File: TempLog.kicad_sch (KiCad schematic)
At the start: 50 parts, among them J1 1.27, 2x5, Male, TH, J2 Conn_01x02, J3 Conn_01x03, J5 Conn_01x02, J6 USB4105-GF-A-060, Q1 DMP6350S, SW1 SMD_4.6x2.8mm_h1.9mm, SW2 SMD_4.6x2.8mm_h1.9mm, U1 STM32F030C8Tx, U2 GD25Q16CSJGR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

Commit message: Added PDFs
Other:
- company: (none) -> Uri Tech
- title: (none) -> Temperature Logger - TempLog - V0

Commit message: Updated project to Kicad 9
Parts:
- U2: value GD25Q16CSJGR -> GD25Q16CSJGR
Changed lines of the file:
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@@
 (kicad_sch
-	(version 20231120)
+	(version 20250114)
 	(generator "eeschema")
-	(generator_version "8.0")
+	(generator_version "9.0")
 	(paper "A3")
 	(title_block
@@
 		(company "Uri Tech")
 	)
+	(rectangle
+		(start 109.982 11.938)
+		(end 210.058 84.836)
+		(stroke
+			(width 0)
+			(type default)
+		)
+		(fill
+			(type none)
+		)
+	)
+	(rectangle
+		(start 11.938 84.836)
+		(end 210.058 160.02)
+		(stroke
+			(width 0)
+			(type default)
+		)
+		(fill
+			(type none)
+		)
+	)
+	(rectangle
+		(start 11.938 11.938)
+		(end 109.982 84.836)
+		(stroke
+			(width 0)
+			(type default)
+		)
+		(fill
+			(type none)
+		)
+	)
+	(rectangle
+		(start 299.974 84.836)
+		(end 407.924 252.984)
+		(stroke
+			(width 0)
+			(type default)
+		)
+		(fill
+			(type none)
+		)
+	)
+	(rectangle
+		(start 11.938 160.02)
+		(end 299.974 284.988)
+		(stroke
+			(width 0)
+			(type default)
+		)
+		(fill
+			(type none)
+		)
+	)
+	(rectangle
+		(start 210.058 84.836)
+		(end 299.974 160.02)
+		(stroke
+			(width 0)
+			(type default)
+		)
+		(fill
+			(type none)
+		)
+	)
+	(rectangle
+		(start 210.058 11.938)
+		(end 299.974 84.836)
+		(stroke
+			(width 0)
+			(type default)
+		)
+		(fill
+			(type none)
+		)
+	)
+	(text "Power Supply"
+		(exclude_from_sim no)
+		(at 108.966 93.218 0)
+		(effects
+			(font
+				(size 1.27 1.27)
+			)
+		)
+	)
+	(text "Programming Interface"
+		(exclude_from_sim no)
+		(at 251.206 94.234 0)
+		(effects
+			(font
+				(size 1.27 1.27)
+			)
+		)
+	)
+	(text "GND"
+		(exclude_from_sim no)
+		(at 46.99 54.61 0)
+		(effects
+			(font
+				(size 1.27 1.27)
+			)
+		)
+	)
+	(text "LEDs"
+		(exclude_from_sim no)
+		(at 154.686 21.844 0)
+		(effects
+			(font
+				(size 1.27 1.27)
+			)
+		)
+	)
+	(text "Microcontroller"
+		(exclude_from_sim no)
+		(at 58.928 167.386 0)
+		(effects
+			(font
+				(size 1.27 1.27)
+			)
+		)
+	)
+	(text "Decoupling Capacitors"
+		(exclude_from_sim no)
+		(at 146.558 231.902 0)
+		(effects
+			(font
+				(size 1.27 1.27)
+			)
+		)
+	)
+	(text "Thermistor Circuit"
+		(exclude_from_sim no)
+		(at 355.346 94.996 0)
+		(effects
+			(font
+				(size 1.27 1.27)
+			)
+		)
+	)
+	(text "TX"
+		(exclude_from_sim no)
+		(at 46.228 52.07 0)
+		(effects
+			(font
+				(size 1.27 1.27)
+			)
+		)
+	)
+	(text "RX"
+		(exclude_from_sim no)
+		(at 46.482 49.53 0)
+		(effects
+			(font
+				(size 1.27 1.27)
+			)
+		)
+	)
+	(text "Boot Modes"
+		(exclude_from_sim no)
+		(at 147.32 178.308 0)
+		(effects
+			(font
+				(size 1.27 1.27)
+			)
+		)
+	)
+	(text "Serial Port"
+		(exclude_from_sim no)
+		(at 60.198 18.288 0)
+		(effects
+			(font
+				(size 1.27 1.27)
+			)
+		)
+	)
+	(text "FLASH"
+		(exclude_from_sim no)
+		(at 249.174 25.4 0)
+		(effects
+			(font
+				(size 1.27 1.27)
+			)
+		)
+	)
+	(text "Reset"
+		(exclude_from_sim no)
+		(at 213.106 182.88 0)
+		(effects
+			(font
+				(size 1.27 1.27)
+			)
+		)
+	)
 	(junction
 		(at 204.47 257.81)
@@
 		)
 	)
-	(rectangle
-		(start 109.982 11.938)
-		(end 210.058 84.836)
-		(stroke
-			(width 0)
-			(type default)
-		)
-		(fill
-			(type none)
-		)
-	)
-	(rectangle
-		(start 11.938 84.836)
-		(end 210.058 160.02)
-		(stroke
-			(width 0)
-			(type default)
-		)
-		(fill
-			(type none)
-		)
-	)
-	(rectangle
-		(start 11.938 11.938)
-		(end 109.982 84.836)
-		(stroke
-			(width 0)
-			(type default)
-		)
-		(fill
-			(type none)
-		)
-	)
-	(rectangle
-		(start 299.974 84.836)
-		(end 407.924 252.984)
-		(stroke
-			(width 0)
-			(type default)
-		)
-		(fill
-			(type none)
-		)
-	)
-	(rectangle
-		(start 11.938 160.02)
-		(end 299.974 284.988)
-		(stroke
-			(width 0)
-			(type default)
-		)
-		(fill
-			(type none)
-		)
-	)
-	(rectangle
-		(start 210.058 84.836)
-		(end 299.974 160.02)
-		(stroke
-			(width 0)
-			(type default)
-		)
-		(fill
-			(type none)
-		)
-	)
-	(rectangle
-		(start 210.058 11.938)
-		(end 299.974 84.836)
-		(stroke
-			(width 0)
-			(type default)
-		)
-		(fill
-			(type none)
-		)
-	)
-	(text "Power Supply"
-		(exclude_from_sim no)
-		(at 108.966 93.218 0)
-		(effects
-			(font
-				(size 1.27 1.27)
-			)
-		)
-	)
-	(text "Programming Interface"
-		(exclude_from_sim no)
-		(at 251.206 94.234 0)
-		(effects
-			(font
-				(size 1.27 1.27)
-			)
-		)
-	)
-	(text "GND"
-		(exclude_from_sim no)
-		(at 46.99 54.61 0)
-		(effects
-			(font
-				(size 1.27 1.27)
-			)
-		)
-	)
-	(text "LEDs"
-		(exclude_from_sim no)
-		(at 154.686 21.844 0)
-		(effects
-			(font
-				(size 1.27 1.27)
-			)
-		)
-	)
-	(text "Microcontroller"
-		(exclude_from_sim no)
-		(at 58.928 167.386 0)
-		(effects
-			(font
-				(size 1.27 1.27)
-			)
-		)
-	)
-	(text "Decoupling Capacitors"
-		(exclude_from_sim no)
-		(at 146.558 231.902 0)
-		(effects
-			(font
-				(size 1.27 1.27)
-			)
-		)
-	)
-	(text "Thermistor Circuit"
-		(exclude_from_sim no)
-		(at 355.346 94.996 0)
-		(effects
-			(font
-				(size 1.27 1.27)
-			)
-		)
-	)
-	(text "TX"
-		(exclude_from_sim no)
-		(at 46.228 52.07 0)
-		(effects
-			(font
-				(size 1.27 1.27)
-			)
-		)
-	)
-	(text "RX"
-		(exclude_from_sim no)
-		(at 46.482 49.53 0)
-		(effects
-			(font
-				(size 1.27 1.27)
-			)
-		)
-	)
-	(text "Boot Modes"
-		(exclude_from_sim no)
-		(at 147.32 178.308 0)
-		(effects
-			(font
-				(size 1.27 1.27)
-			)
-		)
-	)
-	(text "Serial Port"
-		(exclude_from_sim no)
-		(at 60.198 18.288 0)
-		(effects
-			(font
-				(size 1.27 1.27)
-			)
-		)
-	)
-	(text "FLASH"
-		(exclude_from_sim no)
-		(at 249.174 25.4 0)
-		(effects
-			(font
-				(size 1.27 1.27)
-			)
-		)
-	)
-	(text "Reset"
-		(exclude_from_sim no)
-		(at 213.106 182.88 0)
-		(effects
-			(font
-				(size 1.27 1.27)
-			)
-		)
-	)
 	(global_label "USART1_RX"
 		(shape input)
@@
 			)
 		)
-		(property "Value" "GD25Q16CSJGR "
+		(property "Value" "GD25Q16CSJGR"
 			(at 272.796 44.196 0)
 			(effects
@@
 		)
 	)
+	(embedded_fonts no)
 )

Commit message: Removed thermistor circuit and added TMP1075 temperature sensor
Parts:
- removed J2: Conn_01x02, Connector_PinHeader_2.54mm:PinHeader_1x02_P2.54mm_Vertical, symbol Connector:Conn_01x02_Pin
- removed Q1: DMP6350S, SparkFun-Semiconductor-Standard:SOT23-3, symbol SparkFun-DiscreteSemi:Q_PMOS_4.2A_20V
- removed R1, R2: 49.9K, Resistor_SMD:R_0805_2012Metric, symbol Device:R_US
- removed R3: 150K, Resistor_SMD:R_0805_2012Metric, symbol Device:R_US
- removed R4, R5: 10M, Resistor_SMD:R_0805_2012Metric, symbol Device:R_US
- removed TP1, TP3, TP4: TestPoint, TestPoint:TestPoint_Pad_D1.0mm, symbol Connector:TestPoint
- removed U3, U4: LM321, Package_TO_SOT_SMD:SOT-23-5, symbol Amplifier_Operational:LM321
- added R12, R13: 5K, Resistor_SMD:R_0805_2012Metric, symbol Device:R_US
- added U3: TMP1075DGK, Package_SO:VSSOP-8_3x3mm_P0.65mm, symbol Sensor_Temperature:TMP1075DGK
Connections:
- net +3V3: now also R12.1, R13.1, U3.8 (V+)
- net GND: now also U3.3 (ALERT), U3.4 (GND), U3.5 (A2), U3.6 (A1), U3.7 (A0)
- net SDA: now reaches U1.22 (PB11)
- net SDA: now also R12.2, U3.1 (SDA)
- net TEMP_EN: no longer names the net of U1.19 (PB1)
- net THERM_OFST renamed SCL
- net SCL: now also R13.2, U3.2 (SCL)
- net THERM_OUT: no longer names the net of U1.20 (PB2)
- no-connect marks 26 -> 27
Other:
- note added: "Temperature sensor"
- note removed: "Thermistor Circuit"

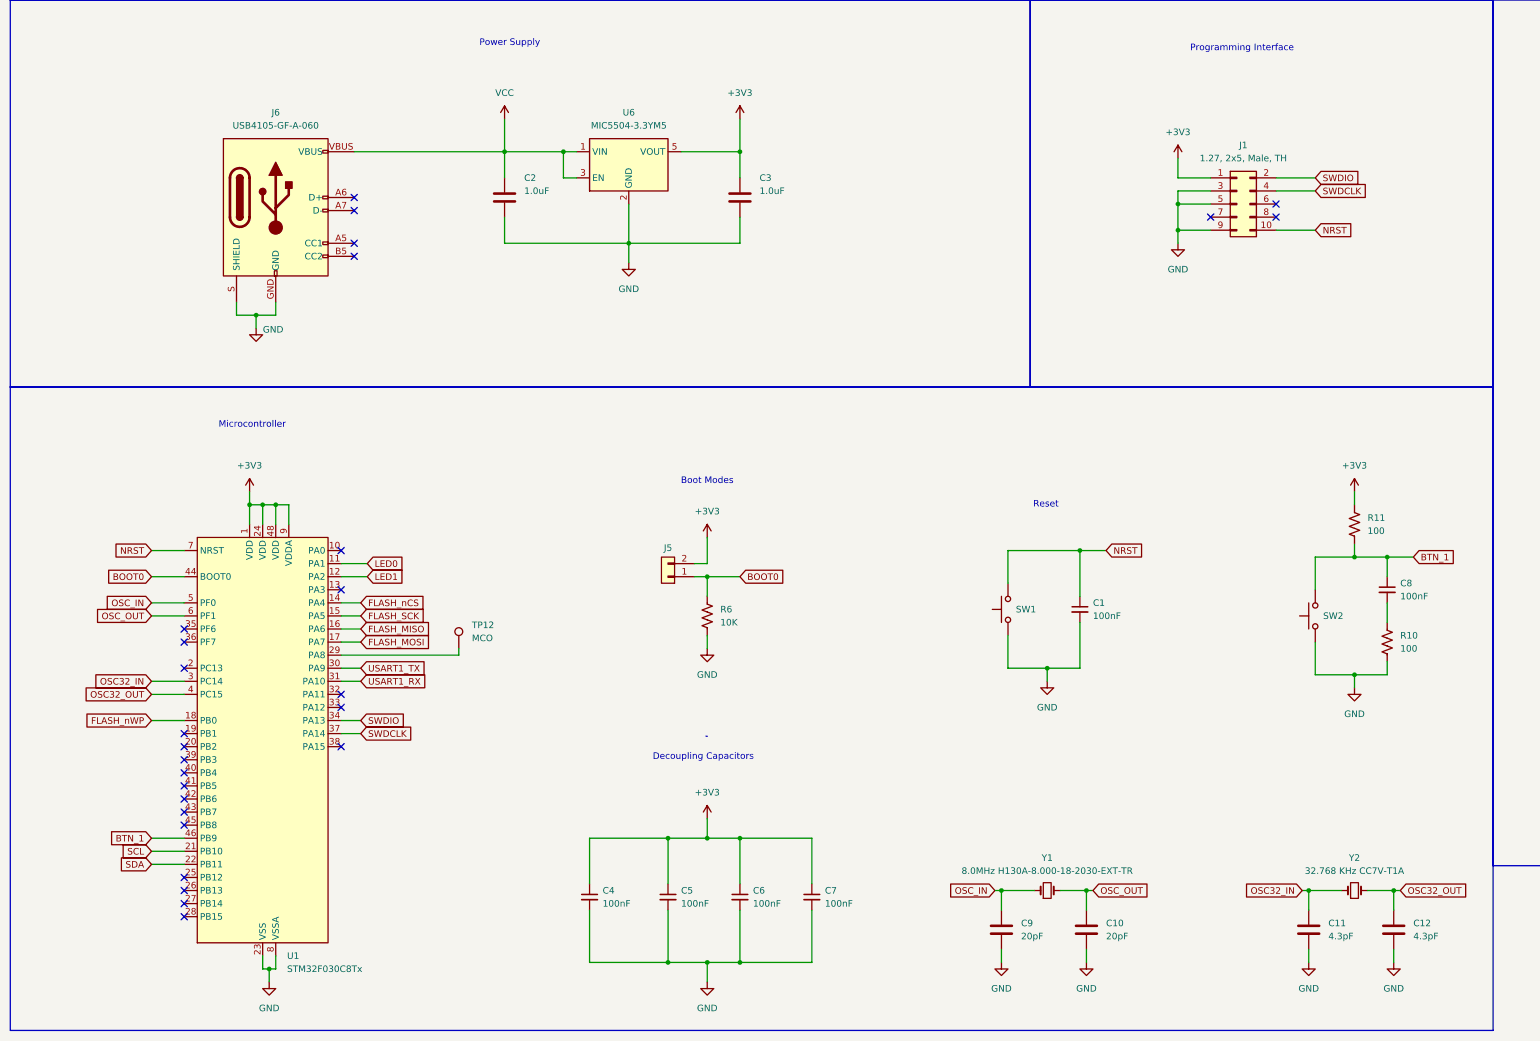
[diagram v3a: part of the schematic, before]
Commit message: updated library links
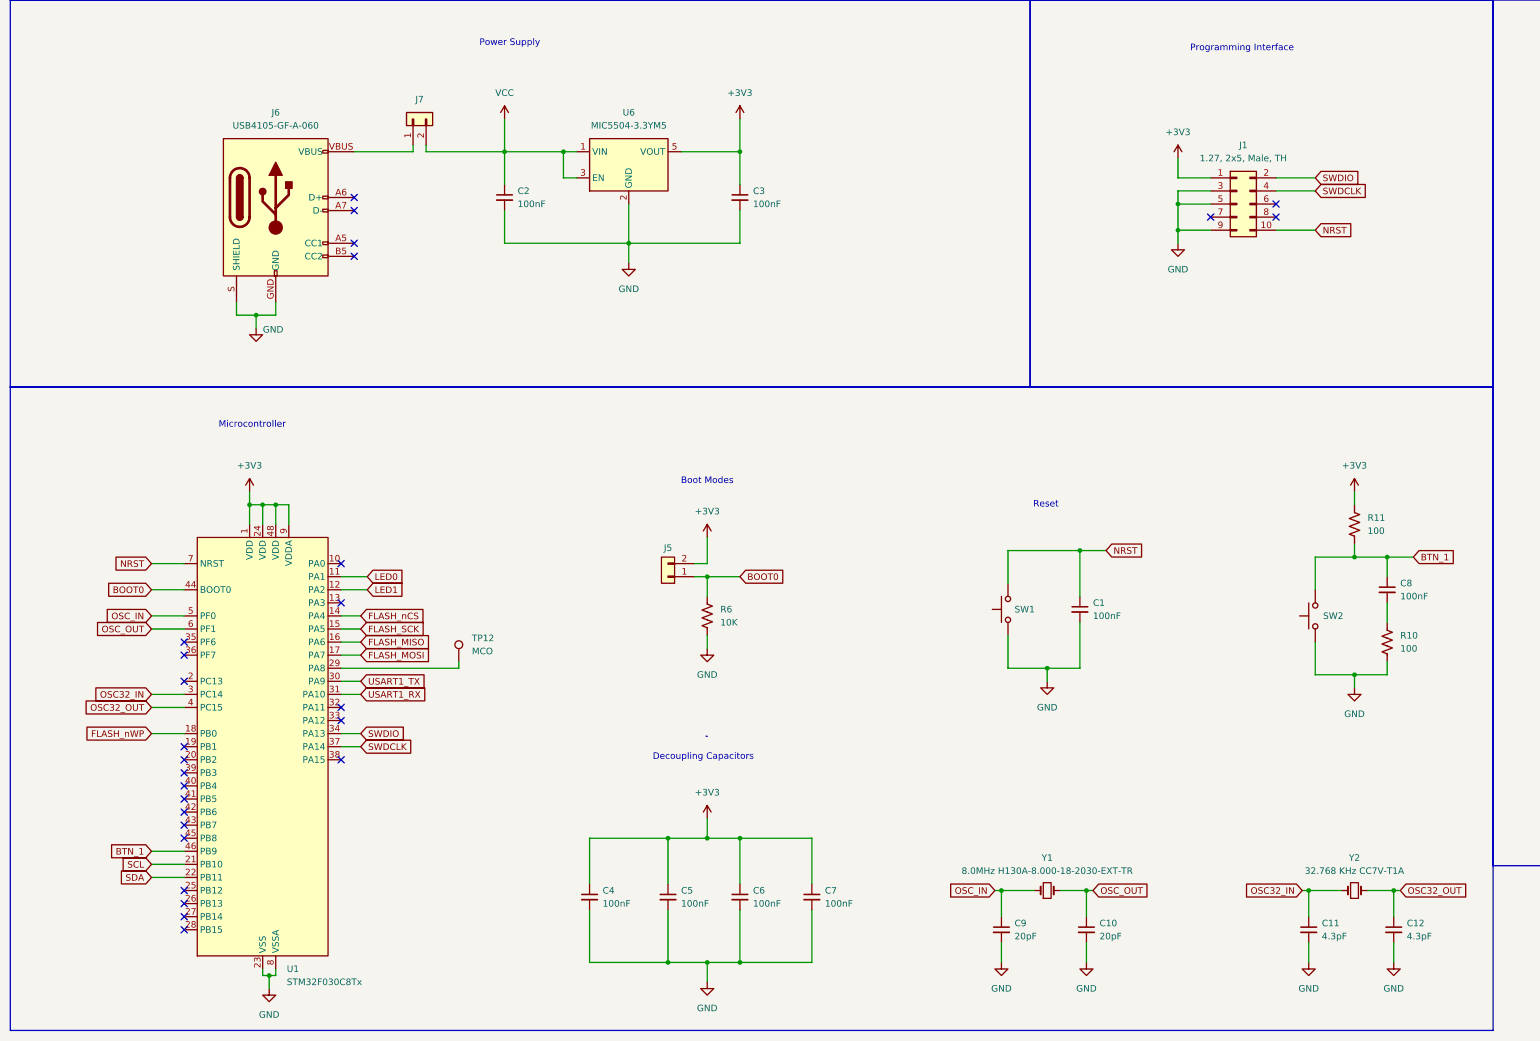
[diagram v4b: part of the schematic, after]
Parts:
- removed C10, C9: 20pF, Capacitor_SMD:C_0805_2012Metric, symbol SparkFun-Capacitor:1.0uF_0805_25V_10%
- removed C11, C12: 4.3pF, Capacitor_SMD:C_0805_2012Metric, symbol SparkFun-Capacitor:1.0uF_0805_25V_10%
- removed C2, C3: 1.0uF, Capacitor_SMD:C_0805_2012Metric, symbol SparkFun-Capacitor:1.0uF_0805_25V_10%
- added C10, C9: 20pF, Capacitor_SMD:C_0805_2012Metric, symbol Device:C_Small
- added C11, C12: 4.3pF, Capacitor_SMD:C_0805_2012Metric, symbol Device:C_Small
- added C2, C3: 100nF, Capacitor_SMD:C_0805_2012Metric, symbol Device:C_Small
- added J7: Conn_01x02, Connector_PinHeader_2.54mm:PinHeader_1x02_P2.54mm_Vertical, symbol Connector_Generic:Conn_01x02
- D1, D2: footprint LED_SMD:LED_0805_2012Metric -> (none)
- SW1, SW2: footprint SparkFun-Switch:Push_SMD_4.6x2.8mm -> SparkFun-Switch:Push_SMD_4.6x2.8mm_h1.9mm
- Y1: footprint Crystal:Crystal_SMD_5032-2Pin_5.0x3.2mm -> SparkFun-Clock:Crystal_SMD_3.2x1.5mm
- Y2: footprint Crystal:Crystal_SMD_MicroCrystal_CC7V-T1A-2Pin_3.2x1.5mm -> SparkFun-Clock:Crystal_SMD_3.2x1.5mm
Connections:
- net +3V3: now also C3.1
- net GND: now also C10.2, C11.2, C12.2, C2.2, C3.2, C9.2
- net OSC32_IN: now also C11.1
- net OSC32_OUT: now also C12.1
- net OSC_IN: now also C9.1
- net OSC_OUT: now also C10.1
- net VCC: now also C2.1, J7.2 (Pin_2); no longer J6.VBUS
- net at J6.A8 (NC): no longer J6.B8 (NC)
- new net: J6.VBUS, J7.1 (Pin_1)
- now unconnected: J6.NC1 (NC), J6.NC2 (NC), J6.NC3 (NC)
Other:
- moved on the sheet: TP12

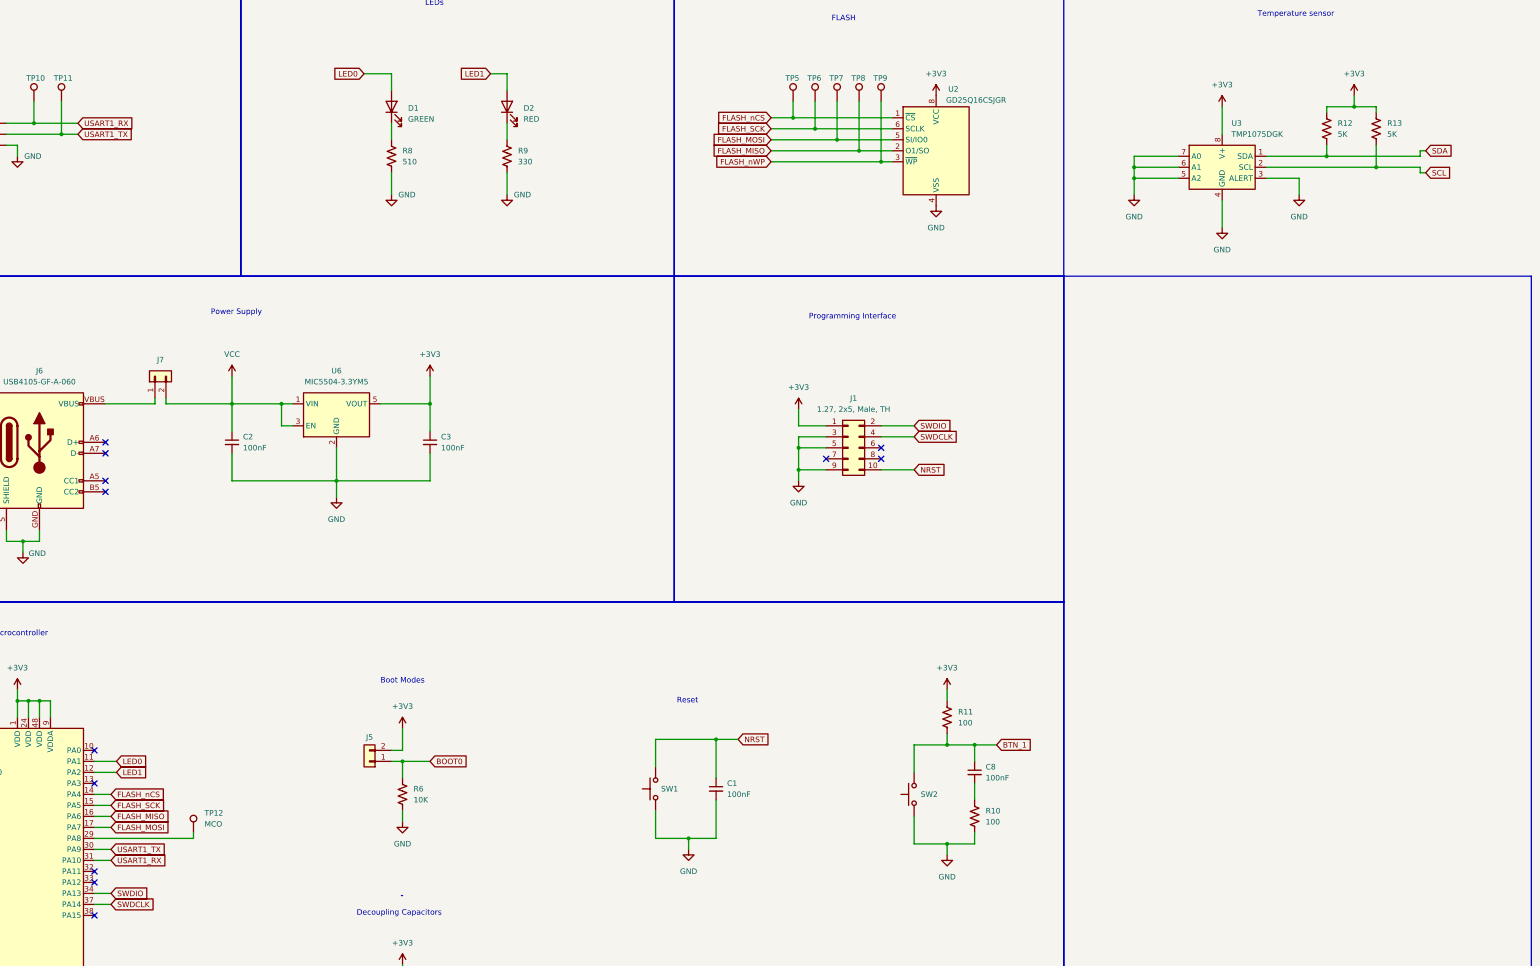
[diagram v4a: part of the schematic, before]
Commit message: Changed board size to 50mm x 40mm and rerouted the nets
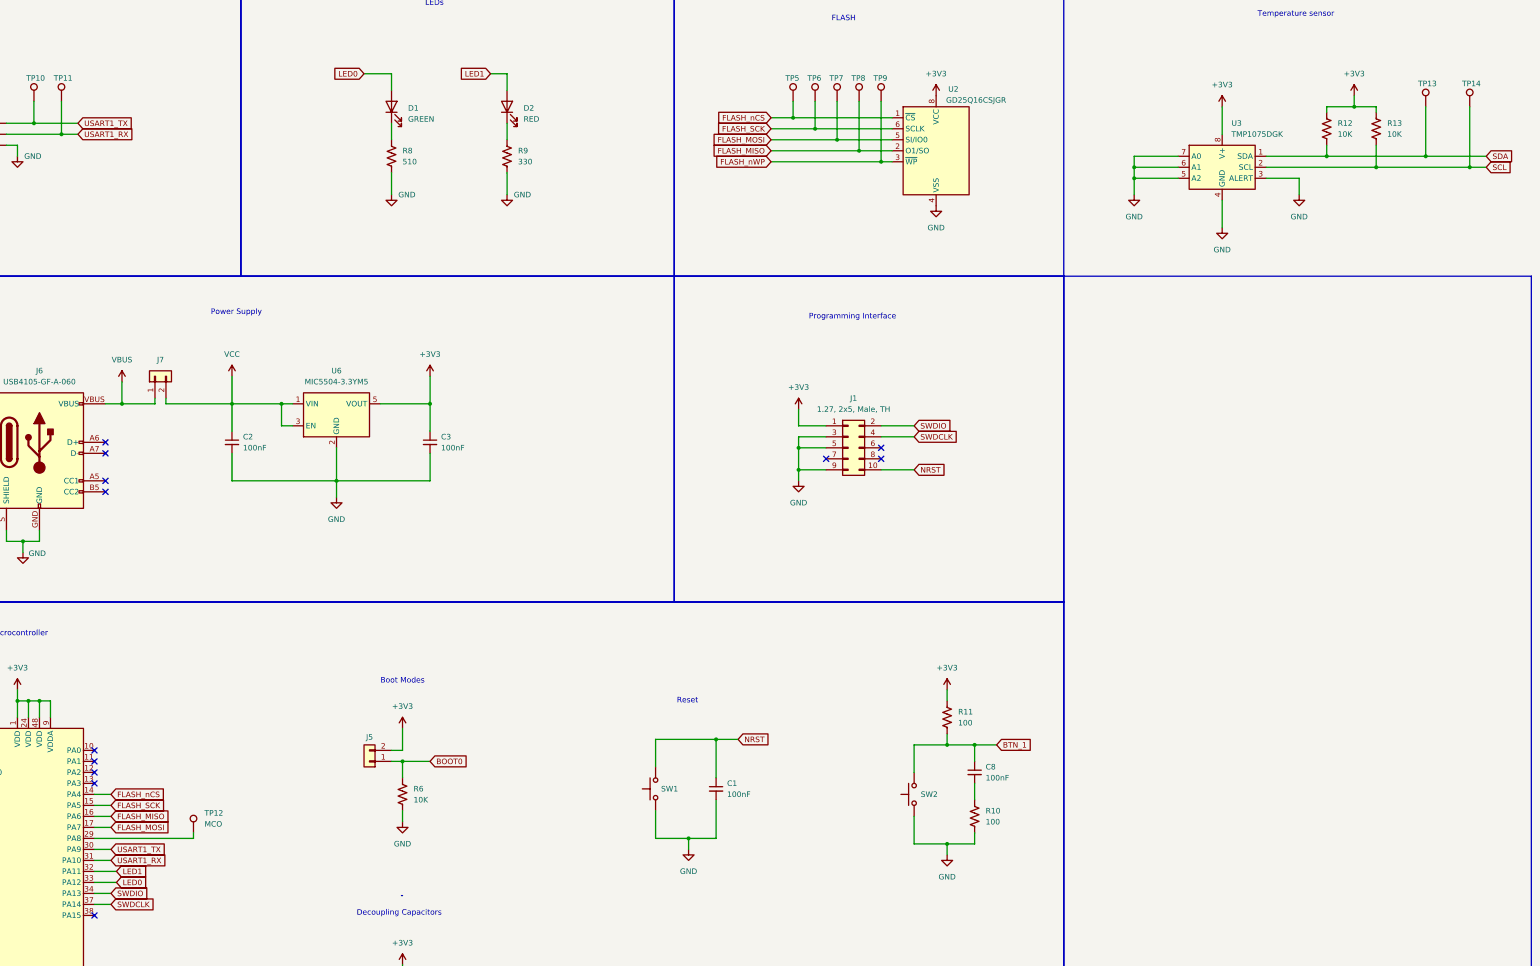
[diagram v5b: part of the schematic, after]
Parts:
- added TP13, TP14: TestPoint, TestPoint:TestPoint_Pad_D1.0mm, symbol Connector:TestPoint
- D1, D2: footprint (none) -> LED_SMD:LED_0805_2012Metric
- J3: footprint Connector_PinSocket_2.54mm:PinSocket_1x03_P2.54mm_Vertical -> Connector_PinHeader_2.54mm:PinHeader_1x03_P2.54mm_Vertical
- R12, R13: value 5K -> 10K
- Y1: footprint SparkFun-Clock:Crystal_SMD_3.2x1.5mm -> Crystal:Crystal_SMD_5032-2Pin_5.0x3.2mm
- Y2: footprint SparkFun-Clock:Crystal_SMD_3.2x1.5mm -> Crystal:Crystal_SMD_MicroCrystal_CC7V-T1A-2Pin_3.2x1.5mm
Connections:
- net LED0: now also U1.33 (PA12); no longer U1.11 (PA1)
- net LED1: now also U1.32 (PA11); no longer U1.12 (PA2)
- net SCL: now also TP14.1
- net SDA: now also TP13.1
- net USART1_RX: now also J3.2 (Pin_2), TP11.1; no longer J3.3 (Pin_3), TP10.1
- net USART1_TX: now also J3.3 (Pin_3), TP10.1; no longer J3.2 (Pin_2), TP11.1
- net VBUS: now reaches J6.VBUS, J7.1 (Pin_1)
